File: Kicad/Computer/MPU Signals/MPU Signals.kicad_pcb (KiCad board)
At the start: 2 copper layers, 127 x 61 mm, 112 parts, among them IC1 FAN2558S38X, IC10 74LVC1G17GV,125, IC11 ATF22V10C-10SU, IC12 ATF22V10C-10SU, IC13 ATF22V10C-10SU, IC14 ATF22V10C-10SU, IC15 74LV1T34GWH, IC16 74LV1T34GWH, IC2 W65C816S6TQG, IC3 74LVC573APW,118, IC4 74LVC4245APW,118, IC5 74LVC04APW,118, IC6 74LVC32APW,118, IC7 74LVC1G08GV,125, IC8 74LVC11PW,112, IC9 NE555DRG4, J1 Conn_01x02_Male, J10 Conn_01x02_Male, J11 Conn_01x10_Male, J12 Conn_01x16_Male, J13 Conn_01x08_Male, J14 Conn_01x12_Male, J15 Conn_01x16_Male, J16 Conn_01x12_Male, J17 Conn_02x05_Counter_Clockwise, J18 Conn_02x05_Counter_Clockwise, J19 SamacSys_Parts:Pin_Header_1.2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, J2 Conn_01x02_Male, J20 Conn_02x05_Counter_Clockwise, J21 SamacSys_Parts:Pin_Header_1.2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, J22 Conn_02x05_Counter_Clockwise, J23 SamacSys_Parts:Pin_Header_1.2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, J24 Conn_02x05_Counter_Clockwise, J3 Conn_01x02_Male, J4 Conn_01x10_Male, J5 Conn_01x02_Male, J6 Conn_01x02_Male, J7 Conn_01x16_Male, J8 Conn_01x02_Male, J9 Conn_01x02_Male

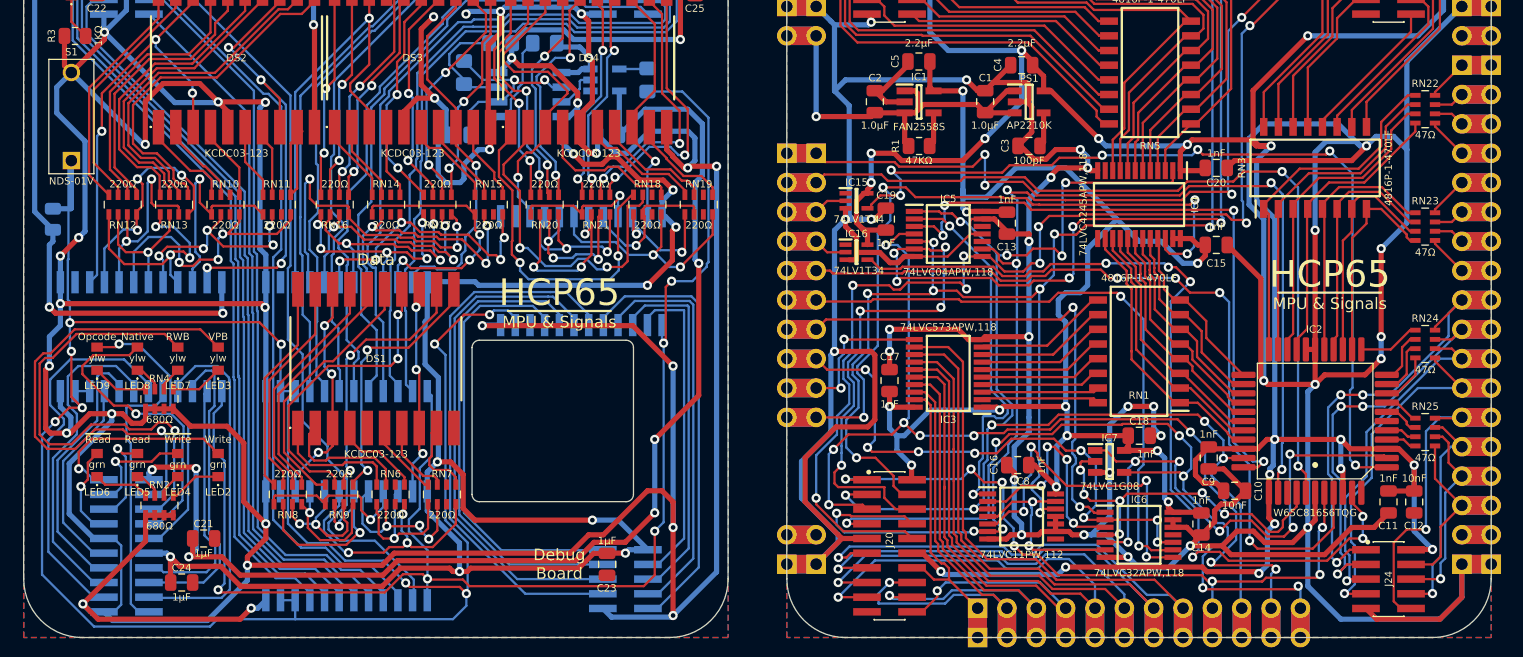
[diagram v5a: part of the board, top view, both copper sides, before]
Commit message: Re-routed Selector State based on new simulation.
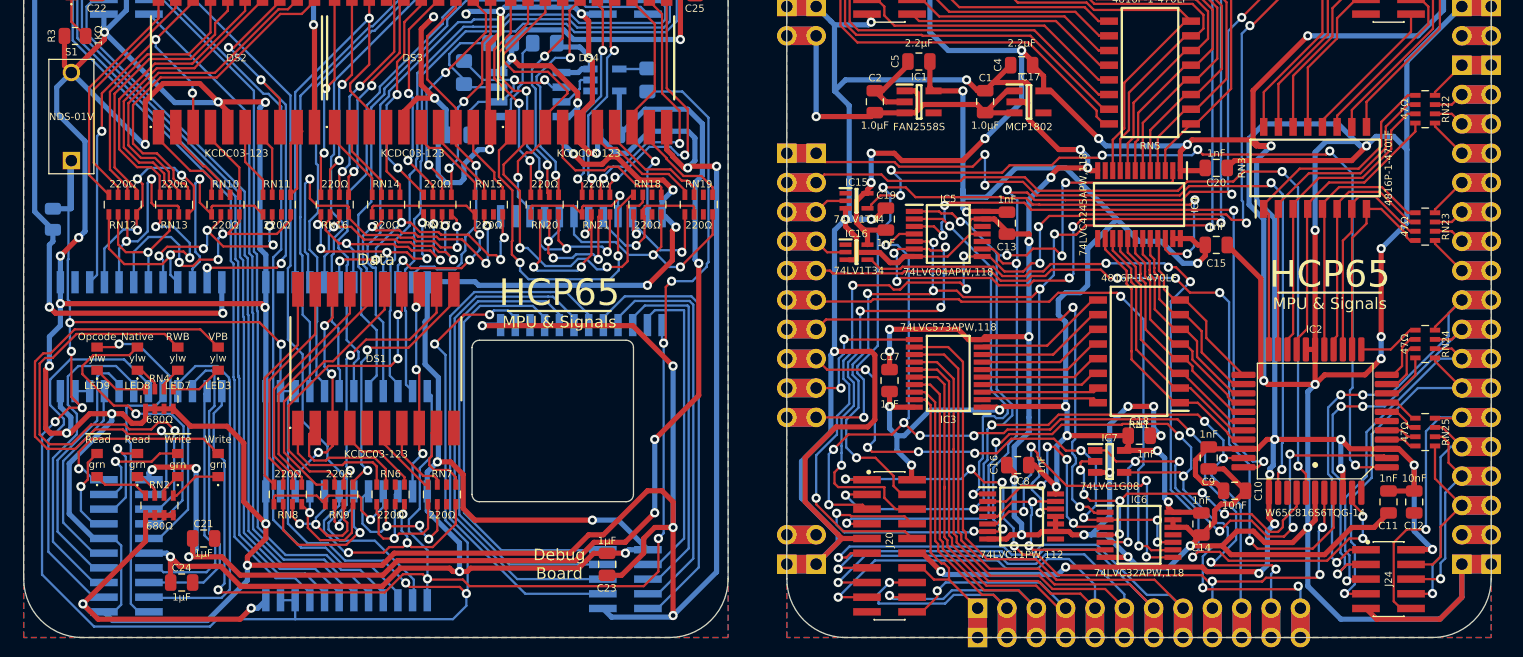
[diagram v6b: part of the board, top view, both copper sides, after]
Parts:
- removed C3: C_0805, SamacSys_Parts:C_0805
- removed PS1: AP2210K-5.0TRG1, SamacSys_Parts:SOT95P282X130-5N
- removed R1: R_0805, SamacSys_Parts:R_0805
- added IC17: MCP1802T-5002I_OT, SamacSys_Parts:SOT95P270X145-5N, F.Cu at (148.0, 89.5)
- IC2: value W65C816S6TQG -> W65C816S6TQG-14
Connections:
- IC1 pad 4: /~{Power Error} -> unconnected-(IC1-Pad4)
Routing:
- net /GND_{TOP}: track 500.3 -> 508.4 mm
- net /Source 5V: track 39.0 -> 36.0 mm
- net /~{Power Error}: track 3.01 -> 0.00 mm
- net Net-(C3-Pad1): track 2.99 -> 0.00 mm
- net /GND: track 503.2 -> 500.8 mm

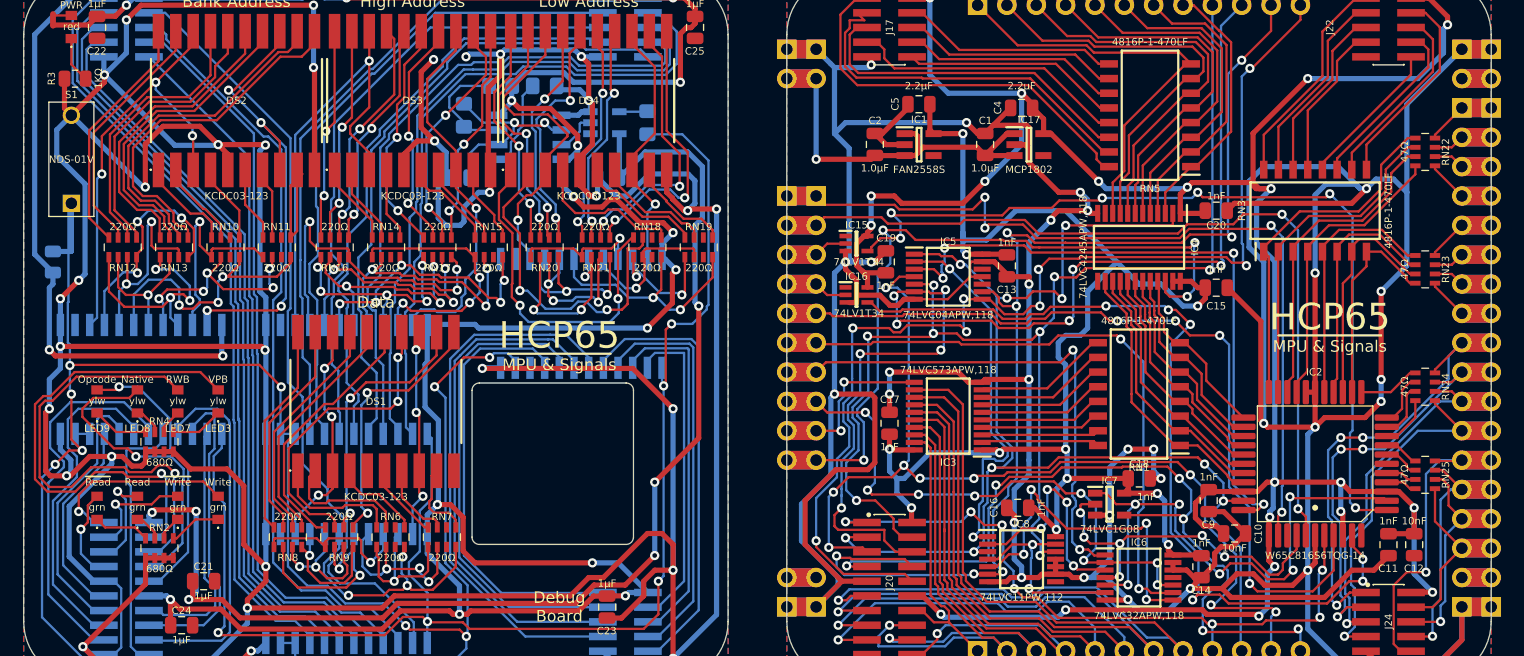
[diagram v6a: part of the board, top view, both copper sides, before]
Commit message: Added a 65C816 stress tester using a Raspberry Pi Pico.
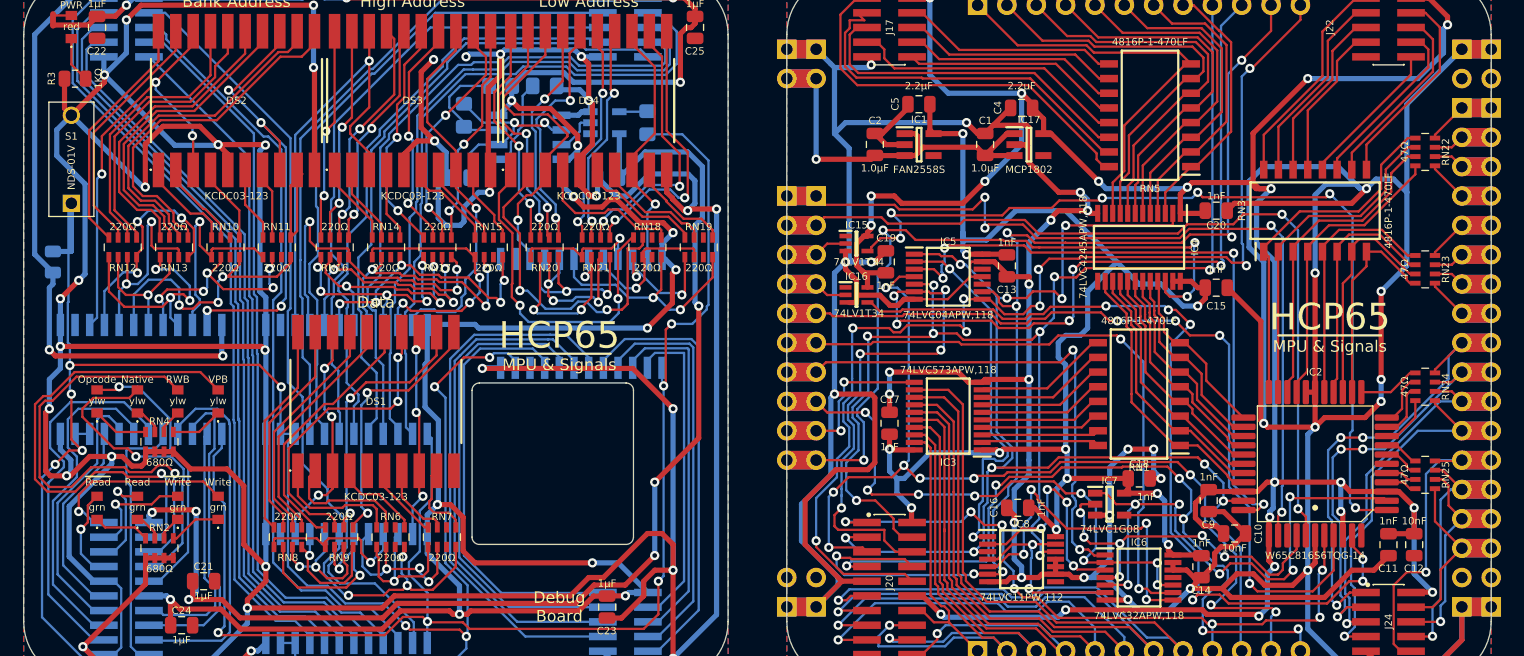
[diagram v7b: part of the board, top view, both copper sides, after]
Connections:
- J10 pad 2: Net-(J10-Pad2) -> unconnected-(J10-Pad2)
- J2 pad 2: Net-(J2-Pad2) -> unconnected-(J2-Pad2)
- J5 pad 2: Net-(J2-Pad2) -> unconnected-(J5-Pad2)
- J6 pad 2: Net-(J6-Pad2) -> unconnected-(J6-Pad2)
- J8 pad 2: Net-(J10-Pad2) -> unconnected-(J8-Pad2)
- J9 pad 2: Net-(J6-Pad2) -> unconnected-(J9-Pad2)
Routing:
- net Net-(J6-Pad2): track 5.08 -> 0.00 mm
- net Net-(J10-Pad2): track 5.08 -> 0.00 mm
- net Net-(J2-Pad2): track 5.08 -> 0.00 mm
- net /Source 5V: track 36.0 -> 38.5 mm

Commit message: Routed Pico Debugger power lines.
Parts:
- R2, R3: value R_0805 -> R_0805_2012Metric
